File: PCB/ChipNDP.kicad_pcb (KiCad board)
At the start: 2 copper layers, 51.3 x 18.3 mm, 15 parts, among them J1 Model_100_System_BUS, U1 AS6C8008_TSOPII, U2 HC238, U3 HC4040, U4 ABT841

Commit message: ChipNDP 007
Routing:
- net VMEM: track 37.8 -> 35.9 mm
- net /RAMRST: track 25.6 -> 26.3 mm, vias 0 -> 2
- net /BUS_A10: track 23.0 -> 23.6 mm
- net /AD3: track 34.2 -> 34.7 mm
- net /(A): track 36.4 -> 36.3 mm, vias 3 -> 2
- net GND: vias 59 -> 54

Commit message: ChipNDP 008
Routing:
- net /BYTE: track 33.8 -> 35.7 mm, vias 4 -> 2
- net /AD4: track 32.8 -> 32.0 mm
- net /AD0: track 38.6 -> 37.9 mm
- net /AD2: track 35.7 -> 35.1 mm
- net /(A): track 36.3 -> 35.8 mm
- net /AD3: track 34.7 -> 34.2 mm
- net GND: vias 54 -> 55

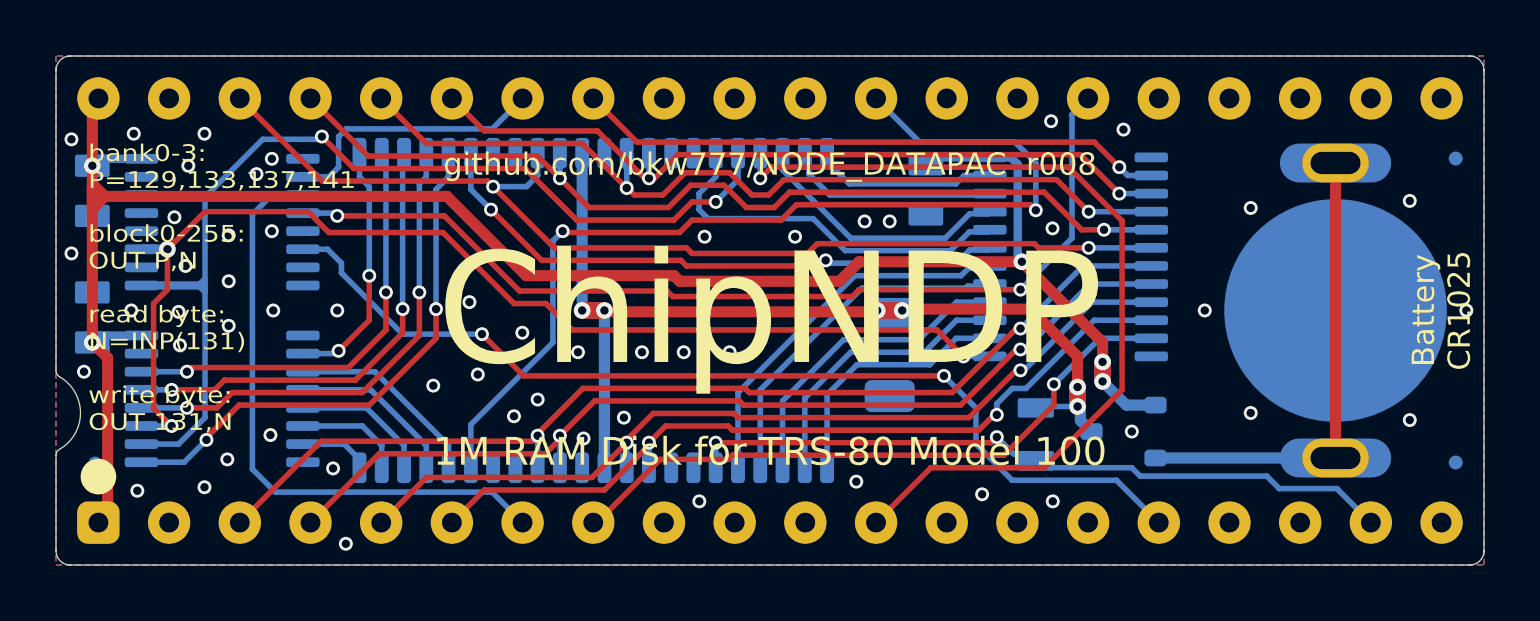
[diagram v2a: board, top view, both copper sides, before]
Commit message: ChipNDP 009 rotate ram chip for /WR /RD
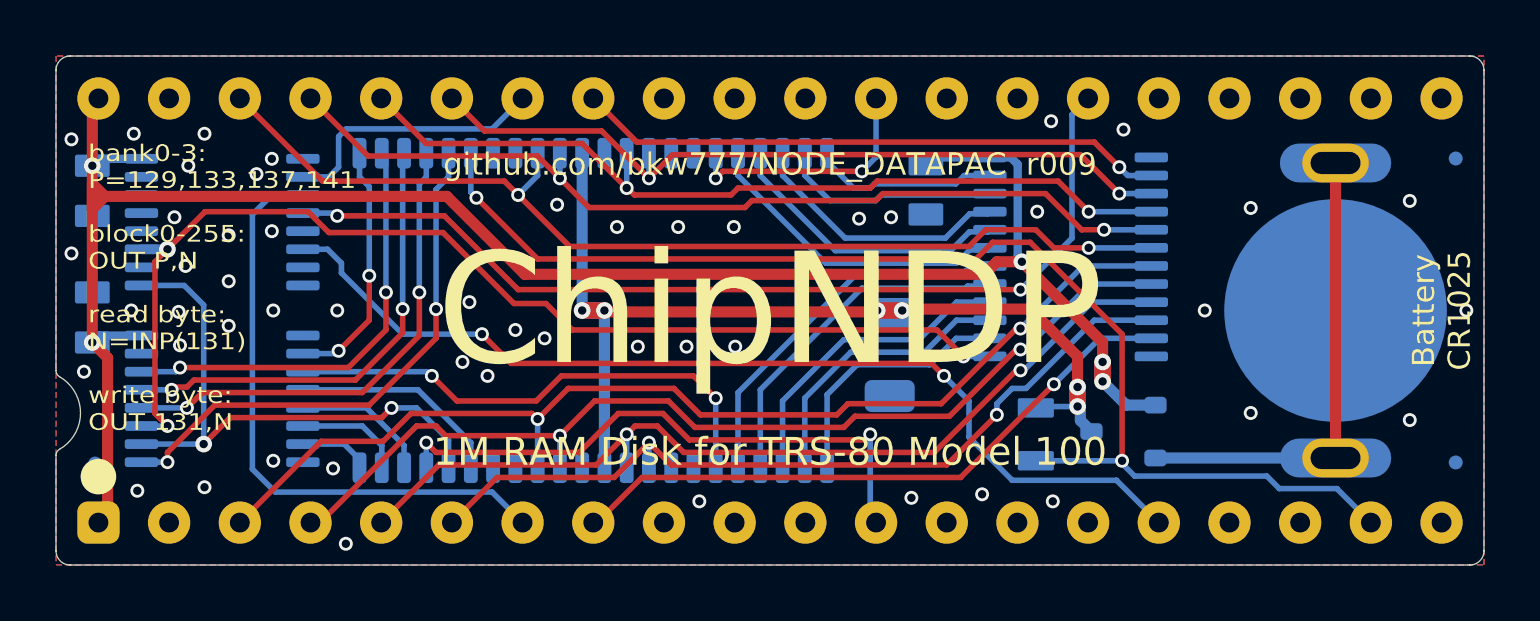
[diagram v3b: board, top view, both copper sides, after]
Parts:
- turned U1 to -90 degrees
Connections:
- U1 pad 1: /A19 -> /A5
- U1 pad 10: /AD4 -> /AD3
- U1 pad 13: /AD2 -> /AD5
- U1 pad 14: /AD0 -> /AD7
- U1 pad 18: /A4 -> /A14
- U1 pad 19: /A6 -> /A13
- U1 pad 2: /A18 -> /A9
- U1 pad 20: /A3 -> /A12
- U1 pad 21: /A2 -> /A11
- U1 pad 22: /A1 -> /A10
- U1 pad 23: /A5 -> /A19
- U1 pad 24: /A9 -> /A18
- U1 pad 25: /A7 -> /A17
- U1 pad 26: /A8 -> /A16
- U1 pad 27: /A0 -> /A15
- U1 pad 28: /A14 -> /A4
- U1 pad 3: /A17 -> /A7
- U1 pad 31: /AD1 -> /AD6
- U1 pad 32: /AD3 -> /AD4
- U1 pad 35: /AD5 -> /AD2
- U1 pad 36: /AD7 -> /AD0
- U1 pad 39: /A13 -> /A6
- U1 pad 4: /A16 -> /A8
- U1 pad 42: /A12 -> /A3
- U1 pad 43: /A11 -> /A2
- U1 pad 44: /A10 -> /A1
- U1 pad 5: /A15 -> /A0
- U1 pad 9: /AD6 -> /AD1
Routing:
- net /~{WR}: track 35.8 -> 9.08 mm
- net /RAMRST: track 25.8 -> 45.0 mm
- net /BYTE: track 35.7 -> 20.6 mm
- net /A4: track 7.13 -> 18.5 mm, vias 0 -> 2
- net /~{RD}: track 31.8 -> 21.3 mm, vias 1 -> 2
- net /A14: track 21.4 -> 11.4 mm, vias 2 -> 0
- net /A13: track 13.6 -> 10.5 mm
- net /A6: track 6.06 -> 7.72 mm
- net /AD0: track 37.9 -> 39.3 mm
- net /AD4: track 32.0 -> 32.9 mm
- net /AD2: track 35.1 -> 36.0 mm
- net /AD5: track 31.7 -> 31.0 mm
- net /AD3: track 34.2 -> 33.5 mm
- net /AD1: track 37.8 -> 37.3 mm
- net GND: vias 55 -> 51

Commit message: ChipNDP 010
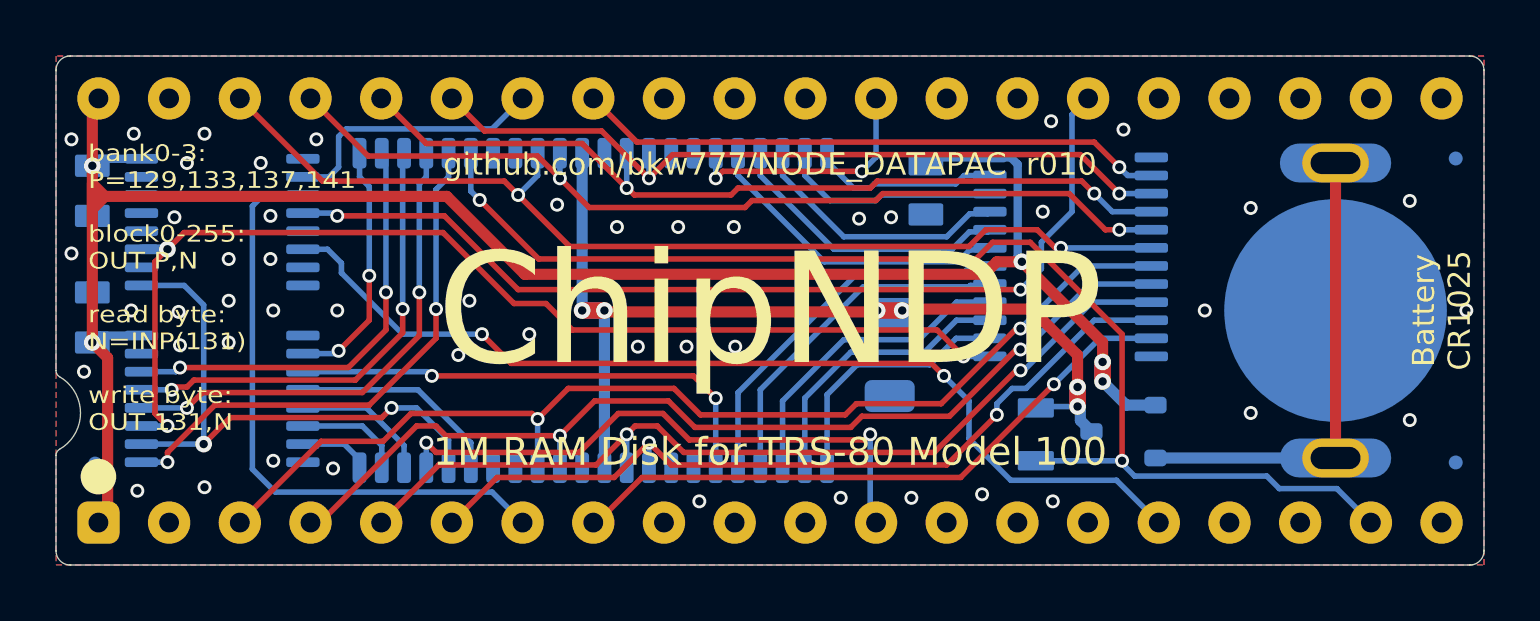
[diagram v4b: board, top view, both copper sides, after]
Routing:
- net /A4: track 18.5 -> 17.7 mm
- net /BLOCK: track 40.9 -> 40.2 mm
- net GND: vias 51 -> 49
